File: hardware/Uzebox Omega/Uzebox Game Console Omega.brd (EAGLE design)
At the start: 100 x 81 mm, 91 parts, among them CON1 USBSERIALSMD, IC1 MCP1700, IC2 7805T, U5 DC IN, U6 23LC1024, X1 A/V

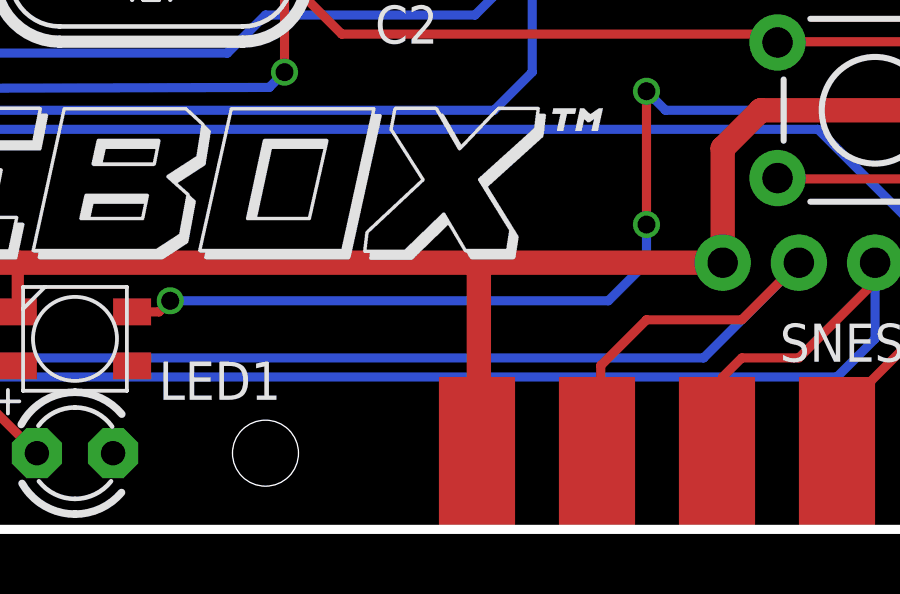
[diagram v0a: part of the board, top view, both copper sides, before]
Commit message: Rename Uzbox F6 to Uzebox Omega
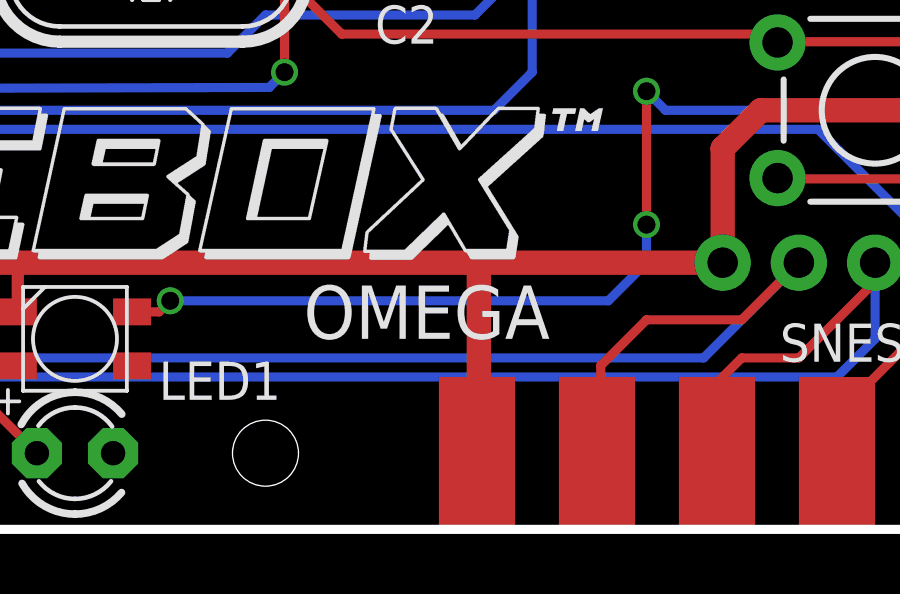
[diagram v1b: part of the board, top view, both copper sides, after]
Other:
- board text added: "OMEGA"
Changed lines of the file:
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@@
 <text x="16.51" y="66.04" size="1.778" layer="21">A/V</text>
 <text x="59.69" y="68.58" size="1.778" layer="21">ISP</text>
+<text x="58.42" y="6.35" size="1.778" layer="21">OMEGA</text>
 </plain>
 <attributes>

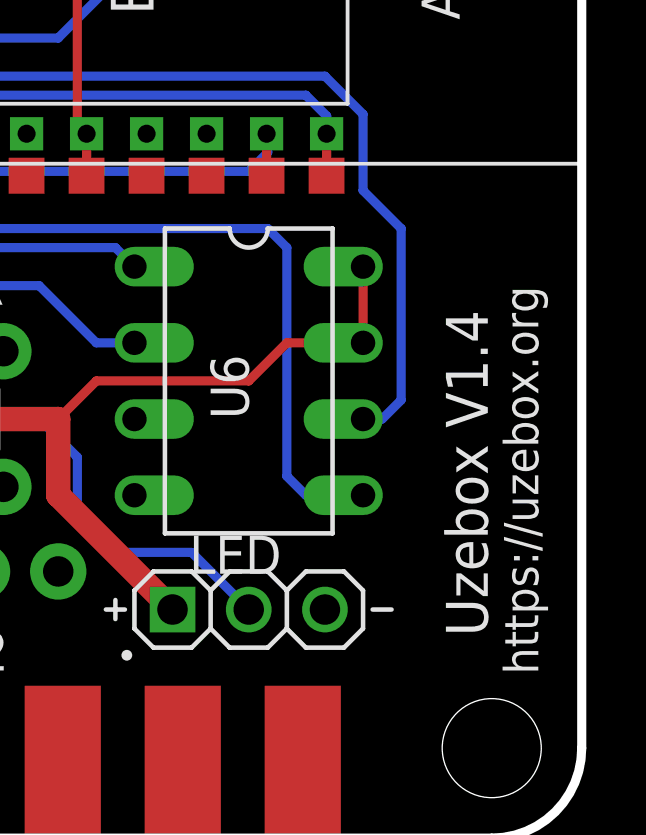
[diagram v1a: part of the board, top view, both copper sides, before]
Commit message: Modified schematic for better readability and corrected silkscreen version
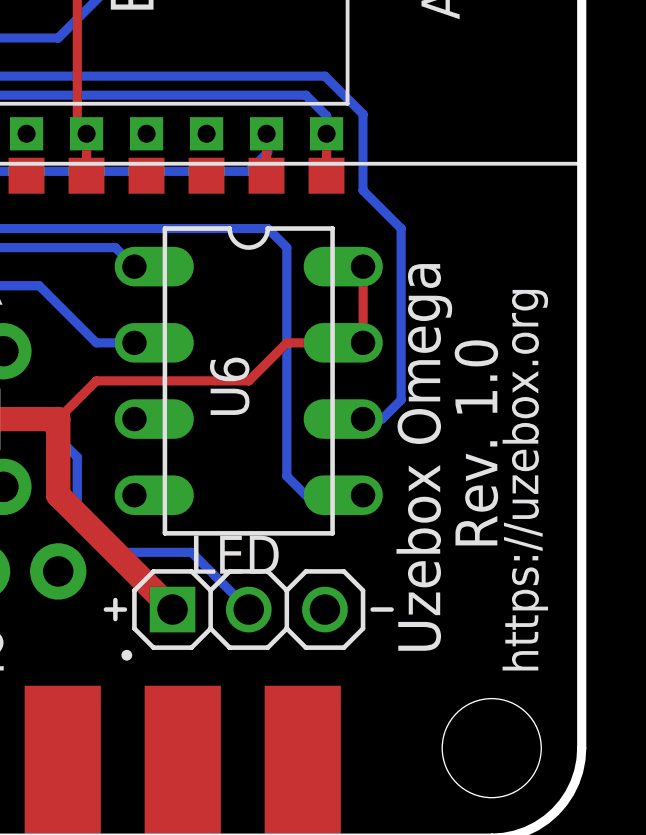
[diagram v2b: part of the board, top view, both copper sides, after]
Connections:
- net N$17 renamed SYNC
- net N$8 renamed CVBS
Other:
- board text added: "Rev. 1.0"
- board text added: "Uzebox Omega"
- board text removed: "Uzebox V1.4"
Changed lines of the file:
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@@
 <wire x1="97" y1="0" x2="3" y2="0" width="0.3048" layer="20"/>
 <text x="2.032" y="59.436" size="1.27" layer="21" font="vector" ratio="10" rot="SR90">7-12VDC</text>
-<text x="96.869" y="6.731" size="1.397" layer="21" font="vector" ratio="7" rot="R90">Uzebox V1.4</text>
+<text x="95.2815" y="6.096" size="1.397" layer="21" font="vector" ratio="7" rot="R90">Uzebox Omega</text>
 <text x="4.064" y="30.734" size="1.27" layer="21">1</text>
 <text x="25.4" y="40.005" size="1.27" layer="21" font="vector" ratio="10" rot="R90">1</text>
@@
 <text x="59.69" y="68.58" size="1.778" layer="21">ISP</text>
 <text x="58.42" y="6.35" size="1.778" layer="21">OMEGA</text>
+<text x="97.1865" y="9.5885" size="1.397" layer="21" font="vector" ratio="7" rot="R90">Rev. 1.0</text>
 </plain>
 <attributes>
@@
 <wire x1="40.485" y1="60.96" x2="41.91" y2="60.96" width="0.3048" layer="1"/>
 </signal>
-<signal name="N$8">
+<signal name="CVBS">
 <contactref element="R20'" pad="2"/>
 <contactref element="VIDEO" pad="SIG"/>
@@
 <wire x1="21.62" y1="72.36" x2="21.62" y2="72.399" width="0.3048" layer="16"/>
 </signal>
-<signal name="N$17">
+<signal name="SYNC">
 <contactref element="X1" pad="4"/>
 <contactref element="JP1" pad="2"/>

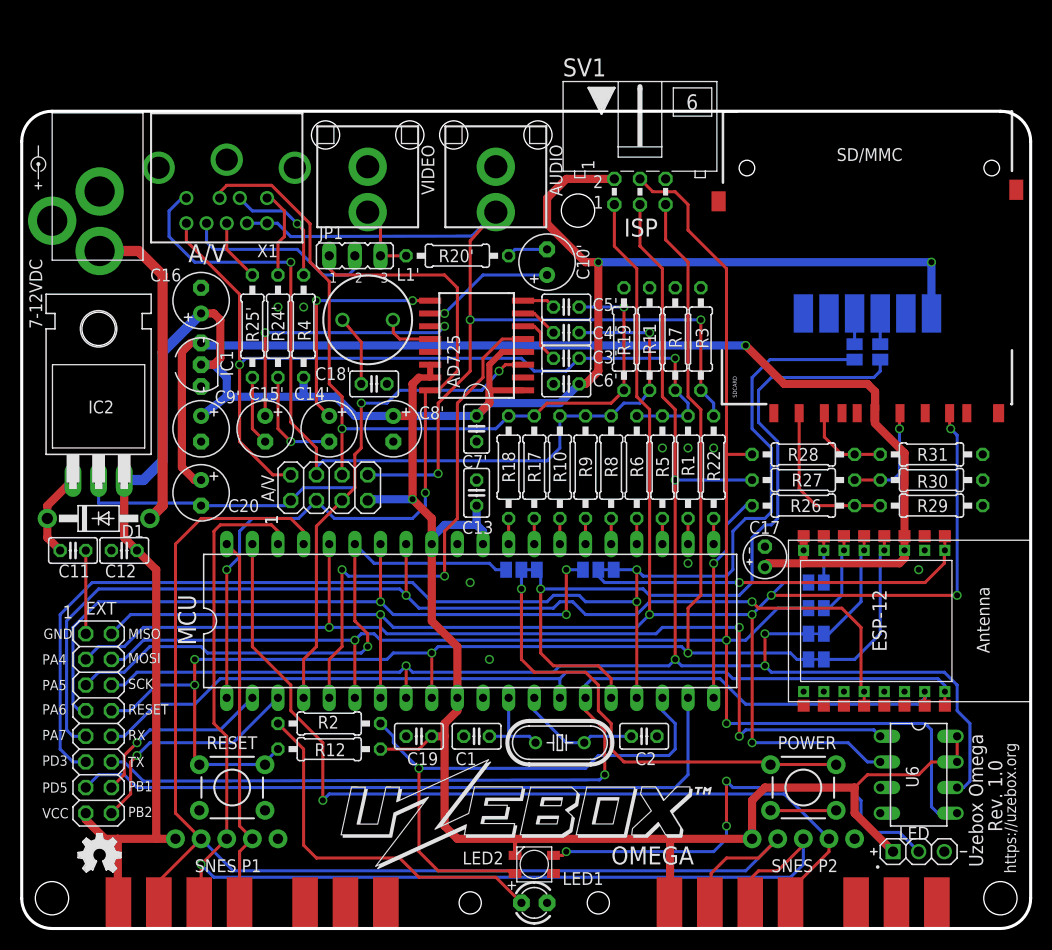
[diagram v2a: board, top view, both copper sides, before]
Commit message: Corrected pinout for Sega Megadrive cables
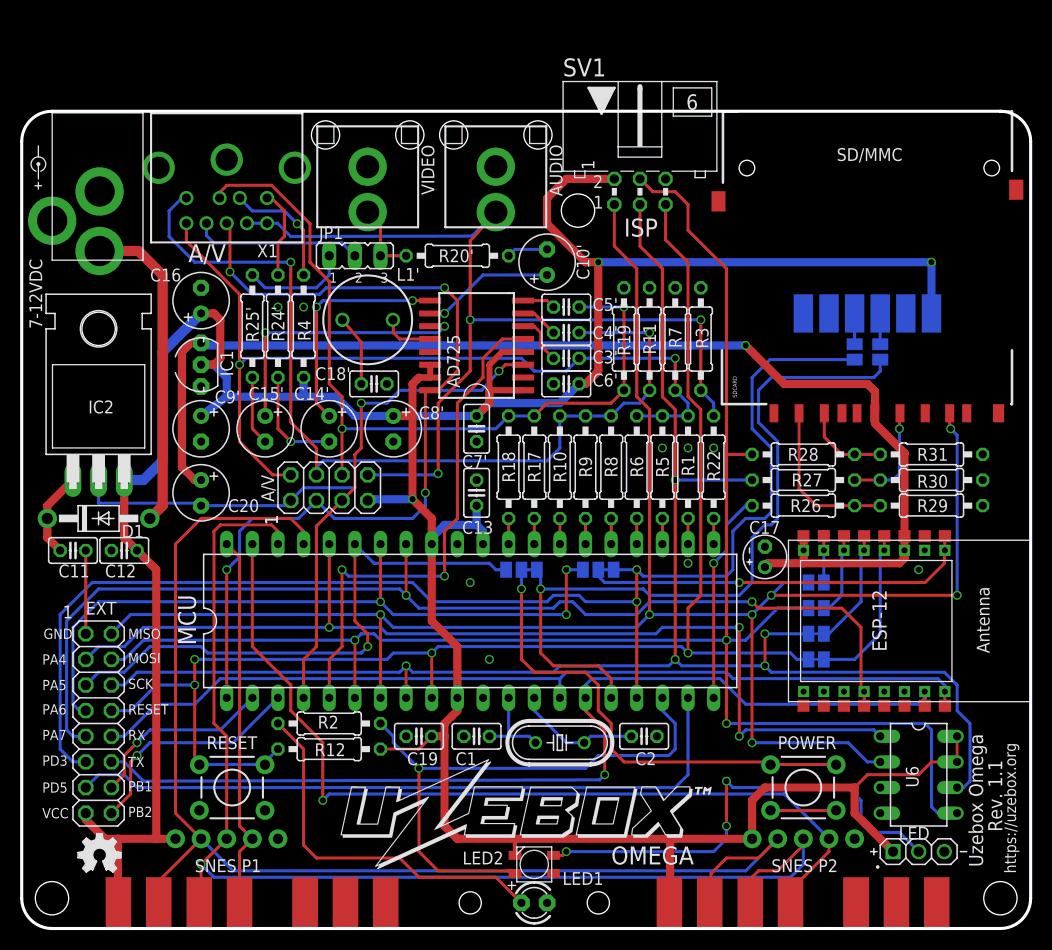
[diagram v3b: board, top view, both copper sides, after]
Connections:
- net SYNC renamed CVBS/LUMA
- net LUMA: now also JP1.1; no longer X1.5
- net VIDEO_SYNC: now also X1.5; no longer JP1.1
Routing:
- net VIDEO_SYNC: track 76.4 -> 89.6 mm, vias 2 -> 4
- net LUMA: track 6.18 -> 10.6 mm
- net CVBS/LUMA: track 19.4 -> 16.8 mm
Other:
- board text added: "Rev. 1.1"
- board text removed: "Rev. 1.0"
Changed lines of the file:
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@@
 <text x="59.69" y="68.58" size="1.778" layer="21">ISP</text>
 <text x="58.42" y="6.35" size="1.778" layer="21">OMEGA</text>
-<text x="97.1865" y="9.5885" size="1.397" layer="21" font="vector" ratio="7" rot="R90">Rev. 1.0</text>
+<text x="97.1865" y="9.5885" size="1.397" layer="21" font="vector" ratio="7" rot="R90">Rev. 1.1</text>
 </plain>
 <attributes>
@@
 <via x="40.005" y="43.18" extent="1-16" drill="0.6"/>
 <via x="20.32" y="35.56" extent="1-16" drill="0.6"/>
-<contactref element="JP1" pad="1"/>
 <wire x1="40.485" y1="53.34" x2="41.275" y2="53.34" width="0.3048" layer="1"/>
 <wire x1="41.275" y1="53.34" x2="43.18" y2="55.245" width="0.3048" layer="1"/>
-<wire x1="43.18" y1="55.245" x2="43.18" y2="63.5" width="0.3048" layer="1"/>
-<wire x1="43.18" y1="63.5" x2="41.91" y2="64.77" width="0.3048" layer="1"/>
-<wire x1="41.91" y1="64.77" x2="31.115" y2="64.77" width="0.3048" layer="1"/>
-<wire x1="31.115" y1="64.77" x2="30.48" y2="65.405" width="0.3048" layer="1"/>
-<wire x1="30.48" y1="66.675" x2="30.48" y2="65.405" width="0.3048" layer="1"/>
+<wire x1="43.18" y1="55.245" x2="43.18" y2="62.23" width="0.3048" layer="1"/>
+<wire x1="43.18" y1="62.23" x2="41.91" y2="63.5" width="0.3048" layer="1"/>
 <wire x1="40.005" y1="43.18" x2="40.005" y2="53.34" width="0.3048" layer="1"/>
 <wire x1="40.005" y1="53.34" x2="40.485" y2="53.34" width="0.3048" layer="1"/>
+<contactref element="X1" pad="5"/>
+<via x="41.91" y="63.5" extent="1-16" drill="0.6"/>
+<wire x1="41.91" y1="63.5" x2="30.1625" y2="63.5" width="0.3048" layer="16"/>
+<wire x1="30.1625" y1="63.5" x2="29.5275" y2="62.865" width="0.3048" layer="16"/>
+<wire x1="29.5275" y1="62.865" x2="22.86" y2="62.865" width="0.3048" layer="16"/>
+<wire x1="22.86" y1="62.865" x2="20.6375" y2="65.0875" width="0.3048" layer="16"/>
+<via x="20.6375" y="65.0875" extent="1-16" drill="0.6"/>
+<wire x1="20.6375" y1="65.0875" x2="20.6375" y2="69.5815" width="0.3048" layer="1"/>
+<wire x1="20.6375" y1="69.5815" x2="20.32" y2="69.899" width="0.3048" layer="1"/>
 </signal>
 <signal name="N$1">
@@
 <contactref element="R20'" pad="2"/>
 <contactref element="VIDEO" pad="SIG"/>
+<wire x1="34.29" y1="71" x2="35.56" y2="69.85" width="0.3048" layer="1"/>
 <contactref element="JP1" pad="3"/>
+<wire x1="35.56" y1="69.85" x2="35.56" y2="66.675" width="0.3048" layer="1"/>
 <wire x1="35.56" y1="66.675" x2="38.1" y2="66.675" width="0.3048" layer="1"/>
-<wire x1="34.29" y1="71" x2="35.56" y2="69.85" width="0.3048" layer="1"/>
-<wire x1="35.56" y1="69.85" x2="35.56" y2="66.675" width="0.3048" layer="1"/>
 </signal>
 <signal name="N$10">
@@
 <contactref element="C14'" pad="+"/>
 <wire x1="30.48" y1="50.8" x2="29.21" y2="52.07" width="0.3048" layer="1"/>
-<wire x1="29.21" y1="52.07" x2="29.21" y2="62.23" width="0.3048" layer="1"/>
-<via x="29.21" y="62.23" extent="1-16" drill="0.6"/>
-<wire x1="29.21" y1="62.23" x2="38.735" y2="62.23" width="0.3048" layer="16"/>
+<wire x1="29.21" y1="52.07" x2="29.21" y2="61.595" width="0.3048" layer="1"/>
+<via x="29.21" y="61.595" extent="1-16" drill="0.6"/>
+<wire x1="29.21" y1="61.595" x2="29.845" y2="62.23" width="0.3048" layer="16"/>
+<wire x1="29.845" y1="62.23" x2="38.735" y2="62.23" width="0.3048" layer="16"/>
 <via x="38.735" y="62.23" extent="1-16" drill="0.6"/>
 <wire x1="38.735" y1="62.23" x2="40.485" y2="62.23" width="0.3048" layer="1"/>
@@
 <signal name="LUMA">
 <contactref element="R25'" pad="1"/>
-<contactref element="X1" pad="5"/>
-<wire x1="22.86" y1="64.77" x2="20.32" y2="67.31" width="0.3048" layer="1"/>
-<wire x1="20.32" y1="69.899" x2="20.32" y2="67.31" width="0.3048" layer="1"/>
+<contactref element="JP1" pad="1"/>
+<wire x1="22.86" y1="64.77" x2="24.13" y2="63.5" width="0.3048" layer="16"/>
+<wire x1="24.13" y1="63.5" x2="29.21" y2="63.5" width="0.3048" layer="16"/>
+<wire x1="29.21" y1="63.5" x2="30.48" y2="64.77" width="0.3048" layer="16"/>
+<wire x1="30.48" y1="64.77" x2="30.48" y2="66.675" width="0.3048" layer="16"/>
 </signal>
 <signal name="N$11">
@@
 <wire x1="21.62" y1="72.36" x2="21.62" y2="72.399" width="0.3048" layer="16"/>
 </signal>
-<signal name="SYNC">
-<contactref element="X1" pad="4"/>
-<contactref element="JP1" pad="2"/>
-<wire x1="19.05" y1="67.31" x2="27.305" y2="67.31" width="0.3048" layer="16"/>
-<wire x1="27.305" y1="67.31" x2="29.845" y2="64.77" width="0.3048" layer="16"/>
-<wire x1="29.845" y1="64.77" x2="32.385" y2="64.77" width="0.3048" layer="16"/>
-<wire x1="32.385" y1="64.77" x2="33.02" y2="65.405" width="0.3048" layer="16"/>
-<wire x1="33.02" y1="65.405" x2="33.02" y2="66.675" width="0.3048" layer="16"/>
-<wire x1="18.32" y1="69.899" x2="18.32" y2="68.04" width="0.3048" layer="16"/>
-<wire x1="18.32" y1="68.04" x2="19.05" y2="67.31" width="0.3048" layer="16"/>
-</signal>
 <signal name="N$3">
 <contactref element="SJ5" pad="2"/>
@@
 <wire x1="86.995" y1="9.525" x2="88.9" y2="7.62" width="0.3048" layer="16"/>
 </signal>
+<signal name="CVBS/LUMA">
+<contactref element="X1" pad="4"/>
+<contactref element="JP1" pad="2"/>
+<wire x1="33.02" y1="66.675" x2="31.75" y2="67.945" width="0.3048" layer="16"/>
+<wire x1="31.75" y1="67.945" x2="19.05" y2="67.945" width="0.3048" layer="16"/>
+<wire x1="19.05" y1="67.945" x2="18.32" y2="68.675" width="0.3048" layer="16"/>
+<wire x1="18.32" y1="69.899" x2="18.32" y2="68.675" width="0.3048" layer="16"/>
+</signal>
 </signals>

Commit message: Changed RCA sockets and disconnect ISP from ESP by default
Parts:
- removed AUDIO, VIDEO: RCA, rca:RCA
- removed U$11: (no value), uzebox:BUMPON
- added K6, K7: RCA-SWMULTICOMP, Thorsten_connectors:CINCH_MULTICOMP
- R1: value 3.16K -> 3k
- R10, R18, R6: value 806 -> 750
- R12: value 301 -> 1.8k
- R17, R9: value 1.58k -> 1.5k
- R2: value 301 -> 470
- R22: value 3.16K -> 3.3k
- R26, R27, R28: value 301 -> 1k8
- R29, R30, R31: value 562 -> 3k3
- R3: value 806 -> 820
- R5: value 1.58K -> 1.5k
- R8: value 3.16k -> 3k
- moved U6 1.80 mm to (88.9, 15.2)
- renumbered SV1 to K5, U5 to K1, X1 to K2
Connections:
- new net AUDIO': K2.8, K2.9, K7.SIGNAL
- new net N$17: ESP-12.5, ESP-12.P$5, SJ1.2
- new net N$18: ESP-12.6, ESP-12.P$6, SJ2.2
- new net N$19: ESP-12.7, ESP-12.P$7, SJ3.2
- new net N$22: JP1.2, K6.SWITCH
- new net N$8: ESP-12.4, ESP-12.P$4, SJ4.2
- net AUDIO: now also K7.SWITCH; no longer AUDIO.SIG, K2.8, K2.9
- net CVBS: no longer VIDEO.SIG
- net CVBS/LUMA: now also K6.SIGNAL; no longer JP1.2
- net GND: now also K6.GND, K7.GND; no longer AUDIO.GND, VIDEO.GND
- net MISO: no longer ESP-12.7, ESP-12.P$7, SJ3.2
- net MOSI: no longer ESP-12.6, ESP-12.P$6, SJ2.2
- net RESET: no longer ESP-12.4, ESP-12.P$4, SJ4.2
- net SCK: no longer ESP-12.5, ESP-12.P$5, SJ1.2
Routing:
- net AUDIO': track 0.00 -> 23.0 mm
- net AUDIO: track 94.3 -> 73.0 mm
- net RESET: track 159.4 -> 141.4 mm
- net N$8: track 0.00 -> 16.5 mm
- net SCK: track 176.0 -> 162.9 mm
- net N$17: track 0.00 -> 11.6 mm
- net N$22: track 0.00 -> 10.4 mm
- net MOSI: track 179.6 -> 169.8 mm
- net N$18: track 0.00 -> 8.25 mm
- net MISO: track 191.7 -> 185.5 mm
- net CVBS: track 7.43 -> 2.54 mm
- net N$19: track 0.00 -> 4.59 mm
- net POWER_SW: track 124.3 -> 121.6 mm
- net N$16: track 0.00 -> 2.54 mm
- net N$14: track 0.00 -> 2.54 mm
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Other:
- board text added: "9V DC"
- board text added: "Audio"
- board text added: "CVBS"
- board text added: "Rev. 1.2"
- board text removed: "Rev. 1.1"
